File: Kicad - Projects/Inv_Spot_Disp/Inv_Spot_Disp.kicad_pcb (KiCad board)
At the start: 2 copper layers, 137.8 x 66 mm, 38 parts, among them J1 PWM_Out, J2 Power_Supply, J3 Current_Sense, J4 Prog, J6 Rail_Sense, SW1 1, SW2 2, SW3 3, SW4 4, SW5 SW_Push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

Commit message: Primeiro Layout - Display
Feito o layout preliminar da placa de display, conferir com o Anderson

Corrigido problema com o layout do transformador (erro no símbolo utilizado levou a inversão dos IGBTs superiores)
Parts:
- added C2: 10u, Capacitor_THT:C_Radial_D10.0mm_H12.5mm_P5.00mm, F.Cu at (103.4, 54.4)
- added C3: 10u, Capacitor_THT:C_Radial_D10.0mm_H12.5mm_P5.00mm, F.Cu at (50.6, 55.5)
- added R11: 20, Resistor_SMD:R_1206_3216Metric_Pad1.30x1.75mm_HandSolder, B.Cu at (106.2, 77.0)
- added R12: 20, Resistor_SMD:R_1206_3216Metric_Pad1.30x1.75mm_HandSolder, B.Cu at (109.5, 77.0)
- added U5: LM358, Package_SO:SOIC-8_3.9x4.9mm_P1.27mm, B.Cu at (49.8, 71.7)
- J6: value Rail_Sense -> Temp_Sense
- moved J2 233.3 mm to (36.9, 52.2)
- moved SW5 221.6 mm to (34.6, 107.6), turned to -90 degrees
- moved C8 216.2 mm to (35.5, 73.5), turned to -90 degrees
- moved J3 207.9 mm to (35.7, 85.5)
- moved R8 194.4 mm to (31.7, 96.9), turned to 90 degrees
- moved R6 186.7 mm to (39.5, 86.3), turned to -90 degrees
- moved J6 186.5 mm to (67.8, 59.5), turned to 90 degrees
- moved R7 186.3 mm to (40.1, 79.5), turned to -90 degrees
- moved C9 182.2 mm to (38.2, 95.8)
- moved R10 172.4 mm to (56.2, 71.8), turned to 0 degrees
- moved C11 170.9 mm to (49.9, 76.9)
- moved R2 169.6 mm to (59.1, 104.5), turned to -90 degrees
- moved U6 164.5 mm to (46.8, 94.3), turned to 0 degrees
- moved C1 164.0 mm to (85.2, 55.6), turned to 180 degrees
- moved R3 159.0 mm to (69.3, 104.5), turned to -90 degrees
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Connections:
- C13 pad 1: 15V -> GND
- C13 pad 2: GND -> 15V
- J4 pad 1: SWWDIO -> Net-(J4-Pin_1)
- J4 pad 2: SWCLK -> Net-(J4-Pin_2)
- SW5 pad 2: GND -> Earth
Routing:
- net GND: track 0.00 -> 499.4 mm, vias 0 -> 2
- net 5V: track 0.00 -> 141.5 mm, vias 0 -> 2
- net 15V: track 0.00 -> 124.1 mm
- net D7: track 0.00 -> 65.3 mm, vias 0 -> 2
- net D4: track 0.00 -> 65.3 mm, vias 0 -> 2
- net D5: track 0.00 -> 63.9 mm, vias 0 -> 2
- net D6: track 0.00 -> 62.1 mm, vias 0 -> 2
- net Display_ADC: track 0.00 -> 54.4 mm
- net Temp_Sense: track 0.00 -> 48.6 mm, vias 0 -> 2
- net Trigger: track 0.00 -> 47.7 mm
- net Current_Sense: track 0.00 -> 46.5 mm
- net Enable: track 0.00 -> 44.2 mm
- net 3V3: track 5.72 -> 47.3 mm
- net RS: track 0.00 -> 39.8 mm
- net Net-(J3-Pin_1): track 0.00 -> 25.1 mm, vias 0 -> 2
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- added copper zone on F.Cu, net GND
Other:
- board size 137.8 x 66 mm -> 137.8 x 68.7 mm

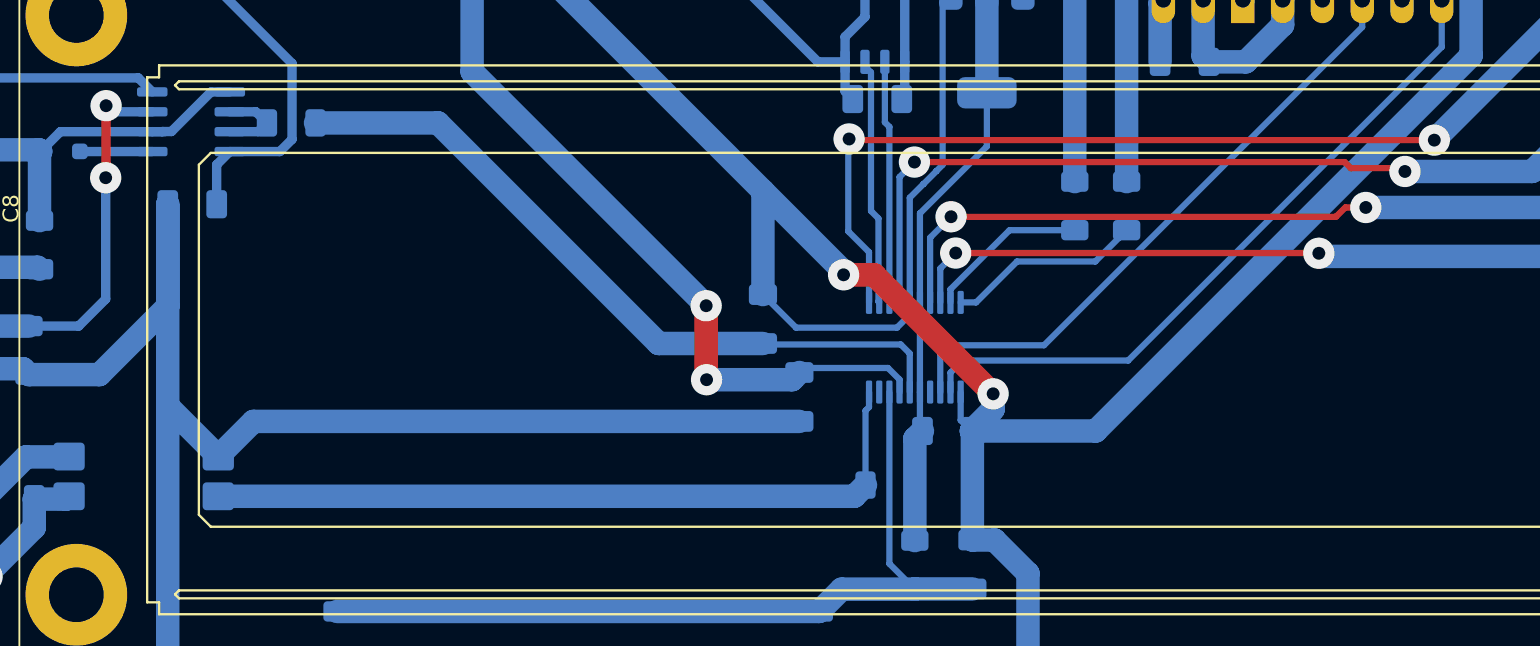
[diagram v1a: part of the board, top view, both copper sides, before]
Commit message: Ajustes Finais
Ajustes em larguras de trilha da camada top

Ajuste do footprint dos capacitores de polipropileno dos IGBTs

Ajuste dos planos de referência
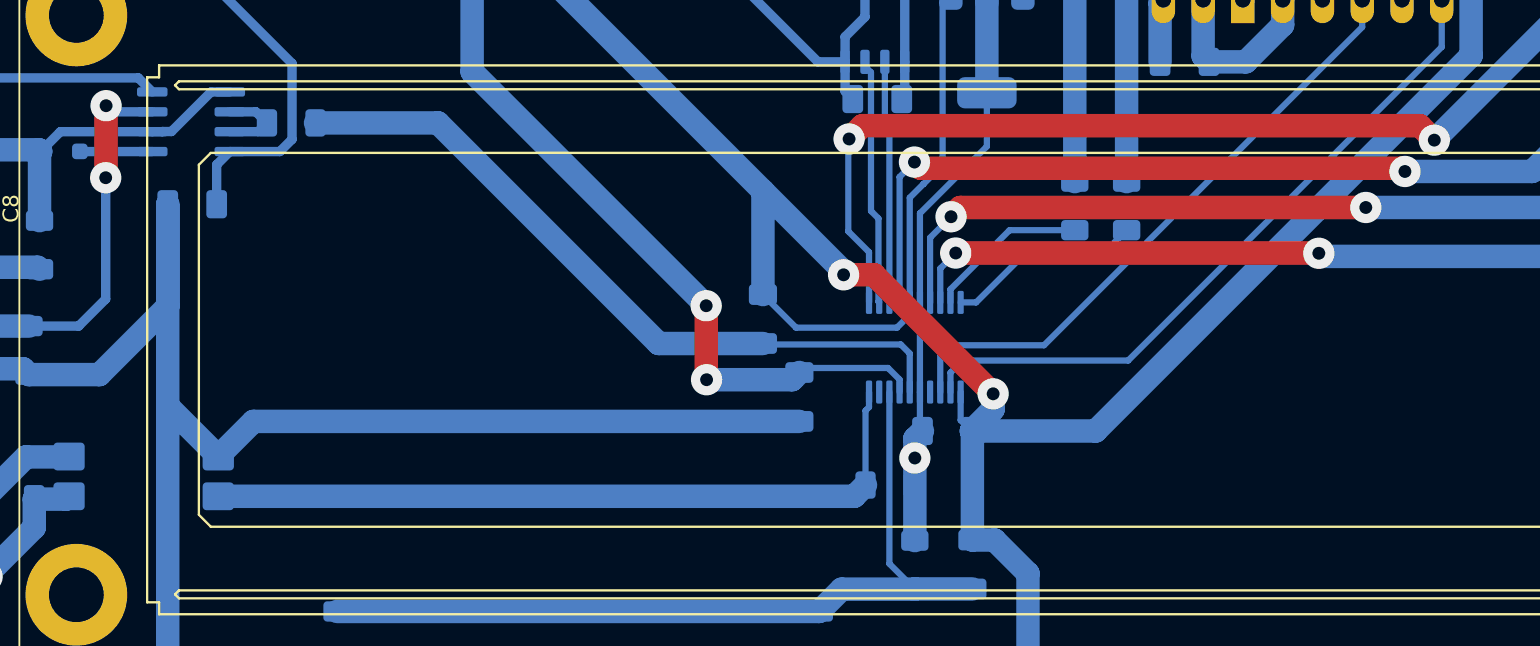
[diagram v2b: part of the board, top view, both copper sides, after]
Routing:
- net D4: track 65.3 -> 66.0 mm
- net 3V3: vias 0 -> 1

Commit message: Ajustes Gerais
Ajustes Gerais
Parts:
- J4: footprint Connector_PinHeader_2.00mm:PinHeader_1x02_P2.00mm_Vertical -> Connector_PinHeader_2.00mm:PinHeader_1x04_P2.00mm_Vertical
- moved J4 1.55 mm to (106.5, 58.7)
- moved J1 1.36 mm to (93.3, 58.9)
- moved C2 1.17 mm to (102.6, 55.2)
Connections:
- J4 pad 1: Net-(J4-Pin_1) -> 3V3
- R11 pad 1: Net-(J4-Pin_1) -> Net-(J4-Pin_2)
- R12 pad 1: Net-(J4-Pin_2) -> Net-(J4-Pin_3)
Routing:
- net Net-(J4-Pin_1): track 18.5 -> 0.00 mm
- net Net-(J4-Pin_3): track 0.00 -> 17.2 mm
- net 3V3: track 47.3 -> 51.5 mm
- net GND: track 499.4 -> 502.5 mm
- net Net-(J1-Pin_2): track 5.01 -> 3.72 mm
- net 5V: track 141.5 -> 140.3 mm
- net D6: track 62.1 -> 63.2 mm
- net RS: track 39.8 -> 40.8 mm
- net Net-(J1-Pin_1): track 4.92 -> 3.94 mm
- net Enable: track 44.2 -> 43.6 mm

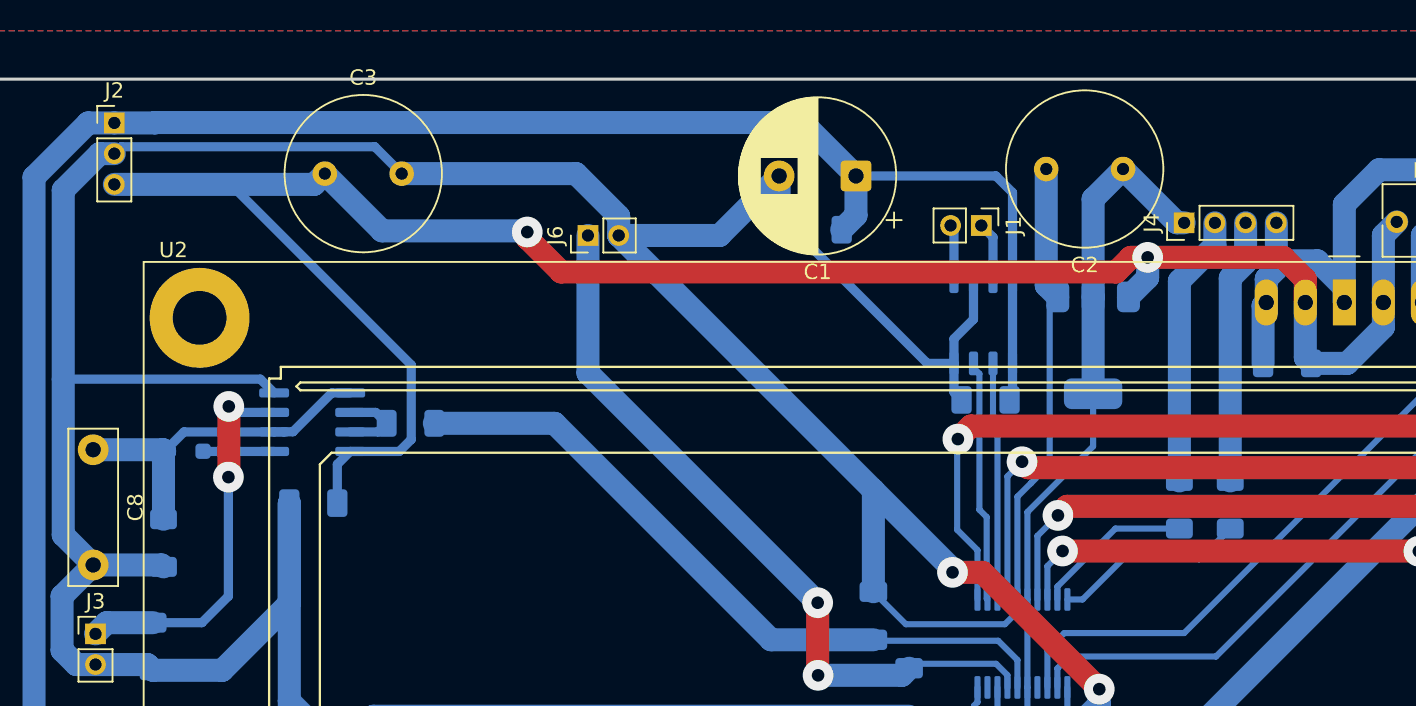
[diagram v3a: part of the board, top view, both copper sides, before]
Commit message: Ajustes Finais
Ajustes finais de footprints e layouts
Considerando aumentar isolamento da trilha T- do IGBT Q2
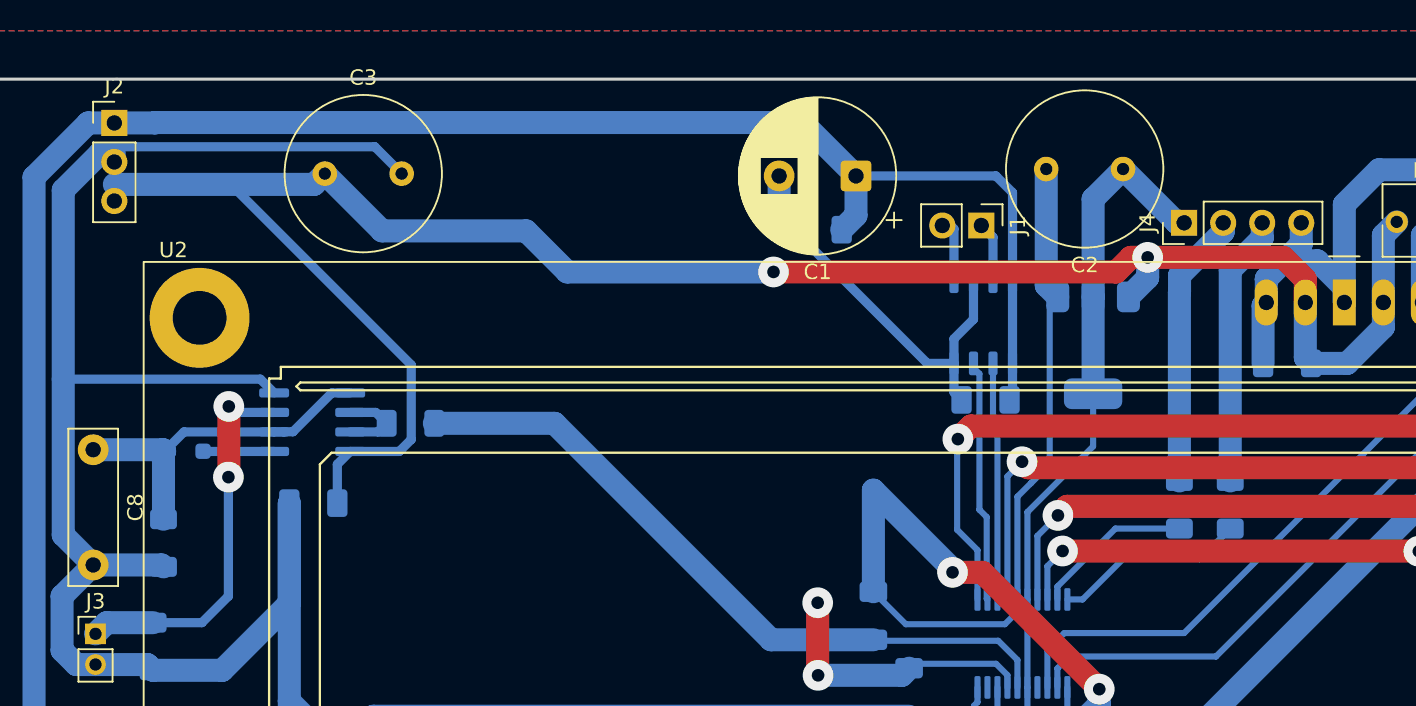
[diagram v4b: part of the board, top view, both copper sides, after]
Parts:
- removed J6: Temp_Sense, Connector_PinHeader_2.00mm:PinHeader_1x02_P2.00mm_Vertical
- J1: footprint Connector_PinHeader_2.00mm:PinHeader_1x02_P2.00mm_Vertical -> Connector_PinHeader_2.54mm:PinHeader_1x02_P2.54mm_Vertical
- J2: footprint Connector_PinHeader_2.00mm:PinHeader_1x03_P2.00mm_Vertical -> Connector_PinHeader_2.54mm:PinHeader_1x03_P2.54mm_Vertical
- J4: footprint Connector_PinHeader_2.00mm:PinHeader_1x04_P2.00mm_Vertical -> Connector_PinHeader_2.54mm:PinHeader_1x04_P2.54mm_Vertical
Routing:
- net GND: track 502.5 -> 451.2 mm
- net Temp_Sense: track 48.6 -> 18.5 mm

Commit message: Ajustes Finais
Ajustes Finais do código, esquemáticos e layouts

Ainda faltam ajustes finos
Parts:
- removed C7: 104, Capacitor_SMD:C_1206_3216Metric_Pad1.33x1.80mm_HandSolder
- added R13: 100, Resistor_SMD:R_1206_3216Metric_Pad1.30x1.75mm_HandSolder, B.Cu at (41.7, 86.3)
- R6: value 56 -> 100
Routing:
- net GND: track 451.2 -> 404.7 mm
- net Temp_Sense: track 18.5 -> 0.00 mm, vias 2 -> 0
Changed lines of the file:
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@@
 			)
 		)
-		(property "Value" "56"
+		(property "Value" "100"
 			(at 0 -1.83 90)
 			(layer "B.Fab")
@@
 	(footprint "Resistor_SMD:R_1206_3216Metric_Pad1.30x1.75mm_HandSolder"
 		(layer "B.Cu")
-		(at 31.7 96.875 90)
+		(at 41.73 86.275 -90)
 		(descr "Resistor SMD 1206 (3216 Metric), square (rectangular) end terminal, IPC-7351 nominal with elongated pad for handsoldering. (Body size source: IPC-SM-782 page 72, https://www.pcb-3d.com/wordpress/wp-content/uploads/ipc-sm-782a_amendment_1_and_2.pdf)")
 		(tags "resistor handsolder")
-		(property "Reference" "R8"
+		(property "Reference" "R13"
 			(at 0 1.83 90)
 			(layer "B.SilkS")
@@
 			)
 		)
-		(property "Value" "1k8"
+		(property "Value" "100"
 			(at 0 -1.83 90)
 			(layer "B.Fab")
@@
 		(duplicate_pad_numbers_are_jumpers no)
 		(fp_line
-			(start -0.727064 -0.91)
-			(end 0.727064 -0.91)
+			(start -0.727064 0.91)
+			(end 0.727064 0.91)
 			(stroke
 				(width 0.12)
@@
 		)
 		(fp_line
-			(start -0.727064 0.91)
-			(end 0.727064 0.91)
+			(start -0.727064 -0.91)
+			(end 0.727064 -0.91)
 			(stroke
 				(width 0.12)
@@
 		)
 		(pad "1" smd roundrect
-			(at -1.55 0 90)
+			(at -1.55 0 270)
 			(size 1.3 1.75)
 			(layers "B.Cu" "B.Mask" "B.Paste")
 			(roundrect_rratio 0.192308)
-			(net "Net-(C9-Pad1)")
+			(net "Net-(J3-Pin_1)")
 			(pintype "passive")
 		)
 		(pad "2" smd roundrect
-			(at 1.55 0 90)
+			(at 1.55 0 270)
 			(size 1.3 1.75)
 			(layers "B.Cu" "B.Mask" "B.Paste")
 			(roundrect_rratio 0.192308)
-			(net "15V")
+			(net "GND")
 			(pintype "passive")
 		)
@@
 		)
 	)
-	(footprint "Capacitor_SMD:C_1206_3216Metric_Pad1.33x1.80mm_HandSolder"
+	(footprint "Resistor_SMD:R_1206_3216Metric_Pad1.30x1.75mm_HandSolder"
 		(layer "B.Cu")
-		(at 86.325 84.275 90)
-		(descr "Capacitor SMD 1206 (3216 Metric), square (rectangular) end terminal, IPC-7351 nominal with elongated pad for handsoldering. (Body size source: IPC-SM-782 page 76, https://www.pcb-3d.com/wordpress/wp-content/uploads/ipc-sm-782a_amendment_1_and_2.pdf)")
-		(tags "capacitor handsolder")
-		(property "Reference" "C12"
-			(at 0 1.85 90)
+		(at 31.7 96.875 90)
+		(descr "Resistor SMD 1206 (3216 Metric), square (rectangular) end terminal, IPC-7351 nominal with elongated pad for handsoldering. (Body size source: IPC-SM-782 page 72, https://www.pcb-3d.com/wordpress/wp-content/uploads/ipc-sm-782a_amendment_1_and_2.pdf)")
+		(tags "resistor handsolder")
+		(property "Reference" "R8"
+			(at 0 1.83 90)
 			(layer "B.SilkS")
 			(effects
@@
 			)
 		)
-		(property "Value" "104"
-			(at 0 -1.85 90)
+		(property "Value" "1k8"
+			(at 0 -1.83 90)
 			(layer "B.Fab")
 			(effects
@@
 			)
 		)
-		(property "Description" "Unpolarized capacitor"
+		(property "Description" "Resistor"
 			(at 0 0 90)
 			(layer "B.Fab")
@@
 			)
 		)
-		(property ki_fp_filters "C_*")
+		(property ki_fp_filters "R_*")
 		(sheetname "/")
 		(sheetfile "Inv_Spot_Disp.kicad_sch")
@@
 		(duplicate_pad_numbers_are_jumpers no)
 		(fp_line
-			(start -0.711252 -0.91)
-			(end 0.711252 -0.91)
+			(start -0.727064 -0.91)
+			(end 0.727064 -0.91)
 			(stroke
 				(width 0.12)
@@
 		)
 		(fp_line
-			(start -0.711252 0.91)
-			(end 0.711252 0.91)
+			(start -0.727064 0.91)
+			(end 0.727064 0.91)
 			(stroke
 				(width 0.12)
@@
 		)
 		(fp_rect
-			(start -2.48 1.15)
-			(end 2.48 -1.15)
+			(start -2.45 1.13)
+			(end 2.45 -1.13)
 			(stroke
 				(width 0.05)
@@
 		)
 		(pad "1" smd roundrect
-			(at -1.5625 0 90)
-			(size 1.325 1.8)
+			(at -1.55 0 90)
+			(size 1.3 1.75)
 			(layers "B.Cu" "B.Mask" "B.Paste")
-			(roundrect_rratio 0.188679)
-			(net "Current_Sense")
+			(roundrect_rratio 0.192308)
+			(net "Net-(C9-Pad1)")
 			(pintype "passive")
 		)
 		(pad "2" smd roundrect
-			(at 1.5625 0 90)
-			(size 1.325 1.8)
+			(at 1.55 0 90)
+			(size 1.3 1.75)
 			(layers "B.Cu" "B.Mask" "B.Paste")
-			(roundrect_rratio 0.188679)
-			(net "GND")
+			(roundrect_rratio 0.192308)
+			(net "15V")
 			(pintype "passive")
 		)
 		(embedded_fonts no)
-		(model "${KICAD10_3DMODEL_DIR}/Capacitor_SMD.3dshapes/C_1206_3216Metric.step"
+		(model "${KICAD10_3DMODEL_DIR}/Resistor_SMD.3dshapes/R_1206_3216Metric.step"
 			(offset
 				(xyz 0 0 0)
@@
 	(footprint "Capacitor_SMD:C_1206_3216Metric_Pad1.33x1.80mm_HandSolder"
 		(layer "B.Cu")
-		(at 88.65 89.25 -90)
+		(at 86.325 84.275 90)
 		(descr "Capacitor SMD 1206 (3216 Metric), square (rectangular) end terminal, IPC-7351 nominal with elongated pad for handsoldering. (Body size source: IPC-SM-782 page 76, https://www.pcb-3d.com/wordpress/wp-content/uploads/ipc-sm-782a_amendment_1_and_2.pdf)")
 		(tags "capacitor handsolder")
-		(property "Reference" "C7"
+		(property "Reference" "C12"
 			(at 0 1.85 90)
 			(layer "B.SilkS")
@@
 		(duplicate_pad_numbers_are_jumpers no)
 		(fp_line
-			(start -0.711252 0.91)
-			(end 0.711252 0.91)
+			(start -0.711252 -0.91)
+			(end 0.711252 -0.91)
 			(stroke
 				(width 0.12)
@@
 		)
 		(fp_line
-			(start -0.711252 -0.91)
-			(end 0.711252 -0.91)
+			(start -0.711252 0.91)
+			(end 0.711252 0.91)
 			(stroke
 				(width 0.12)
@@
 		)
 		(pad "1" smd roundrect
-			(at -1.5625 0 270)
+			(at -1.5625 0 90)
 			(size 1.325 1.8)
 			(layers "B.Cu" "B.Mask" "B.Paste")
 			(roundrect_rratio 0.188679)
-			(net "Temp_Sense")
+			(net "Current_Sense")
 			(pintype "passive")
 		)
 		(pad "2" smd roundrect
-			(at 1.5625 0 270)
+			(at 1.5625 0 90)
 			(size 1.325 1.8)
 			(layers "B.Cu" "B.Mask" "B.Paste")
@@
 	)
 	(segment
+		(start 91.475 81.45)
+		(end 87.5875 81.45)
+		(width 1.5)
+		(layer "B.Cu")
+		(net "GND")
+	)
+	(segment
 		(start 92.84 64.98)
 		(end 92.84 62.5)
@@
 	)
 	(segment
-		(start 91.475 81.25)
-		(end 91.475 81.45)
-		(width 1.5)
-		(layer "B.Cu")
-		(net "GND")
-	)
-	(segment
 		(start 95.7 84.009878)
 		(end 94.884878 84.825)
@@
 	)
 	(segment
-		(start 86.325 76.1)
-		(end 91.475 81.25)
-		(width 1.5)
-		(layer "B.Cu")
-		(net "GND")
-	)
-	(segment
 		(start 113.075 61.175)
 		(end 115.225 61.175)
@@
 	)
 	(segment
-		(start 86.325 82.7125)
-		(end 86.325 76.1)
-		(width 1.5)
-		(layer "B.Cu")
-		(net "GND")
-	)
-	(segment
-		(start 53.7825 90.8125)
-		(end 51.54 93.055)
-		(width 1.5)
-		(layer "B.Cu")
-		(net "GND")
-	)
-	(segment
 		(start 127.135 60.31)
 		(end 127.135 63.885)
@@
 	)
 	(segment
-		(start 88.65 90.8125)
-		(end 53.7825 90.8125)
-		(width 1.5)
-		(layer "B.Cu")
-		(net "GND")
-	)
-	(segment
 		(start 80.192677 55.65)
 		(end 80.192677 58.205177)
@@
 	)
 	(segment
+		(start 87.5875 81.45)
+		(end 86.325 82.7125)
+		(width 1.5)
+		(layer "B.Cu")
+		(net "GND")
+	)
+	(segment
 		(start 95.7 83.2125)
 		(end 95.7 76.525)
@@
 	)
 	(segment
-		(start 82.7 83.425)
-		(end 82.7 88.125)
-		(width 1.5)
-		(layer "F.Cu")
-		(net "Temp_Sense")
-	)
-	(segment
-		(start 82.7 88.125)
-		(end 82.725 88.15)
-		(width 1.5)
-		(layer "F.Cu")
-		(net "Temp_Sense")
-	)
-	(via
-		(at 82.7 83.425)
-		(size 2)
-		(drill 0.82)
-		(layers "F.Cu" "B.Cu")
-		(net "Temp_Sense")
-	)
-	(via
-		(at 82.725 88.15)
-		(size 2)
-		(drill 0.82)
-		(layers "F.Cu" "B.Cu")
-		(net "Temp_Sense")
-	)
-	(segment
-		(start 88.65 87.6875)
-		(end 88.9375 87.4)
-		(width 0.4)
-		(layer "B.Cu")
-		(net "Temp_Sense")
-	)
-	(segment
-		(start 88.9375 87.4)
-		(end 94.309878 87.4)
-		(width 0.4)
-		(layer "B.Cu")
-		(net "Temp_Sense")
-	)
-	(segment
-		(start 94.309878 87.4)
-		(end 95.05 88.140122)
-		(width 0.4)
-		(layer "B.Cu")
-		(net "Temp_Sense")
-	)
-	(segment
-		(start 82.725 88.15)
-		(end 88.1875 88.15)
-		(width 1.5)
-		(layer "B.Cu")
-		(net "Temp_Sense")
-	)
-	(segment
-		(start 88.1875 88.15)
-		(end 88.65 87.6875)
-		(width 1.5)
-		(layer "B.Cu")
-		(net "Temp_Sense")
-	)
-	(segment
-		(start 95.05 88.140122)
-		(end 95.05 88.9375)
-		(width 0.4)
-		(layer "B.Cu")
-		(net "Temp_Sense")
-	)
-	(segment
